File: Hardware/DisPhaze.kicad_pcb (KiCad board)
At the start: 2 copper layers, 60 x 110 mm, 78 parts, among them J1 SWD_Header, J2 PItch_In, J3 PD1_Amt_In, J4 PD2_Amt_In, J5 VCA_In, J6 DAC1_Out, J7 DAC2_Out, J8 Eurorack_16_pin_power, SW1 DAC1_RingMod_Switch, SW2 DAC2_Mix_Switch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

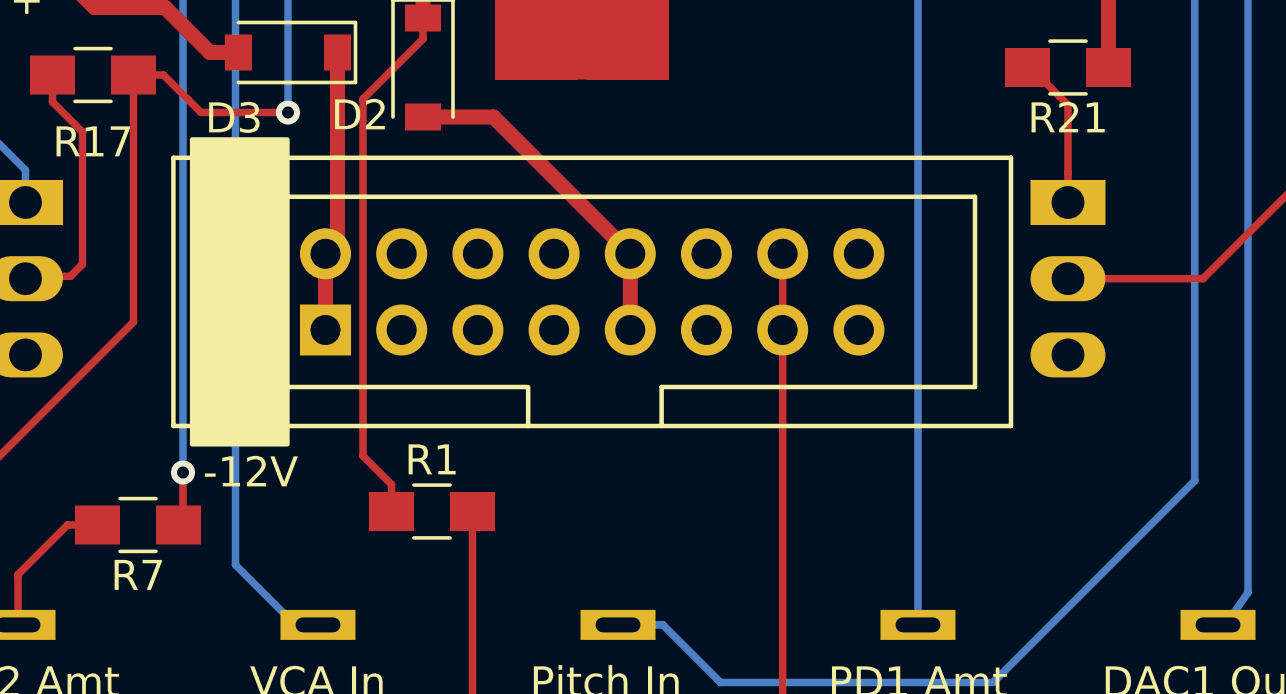
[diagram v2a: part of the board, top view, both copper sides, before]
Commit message: Added 3d models to PCB layout
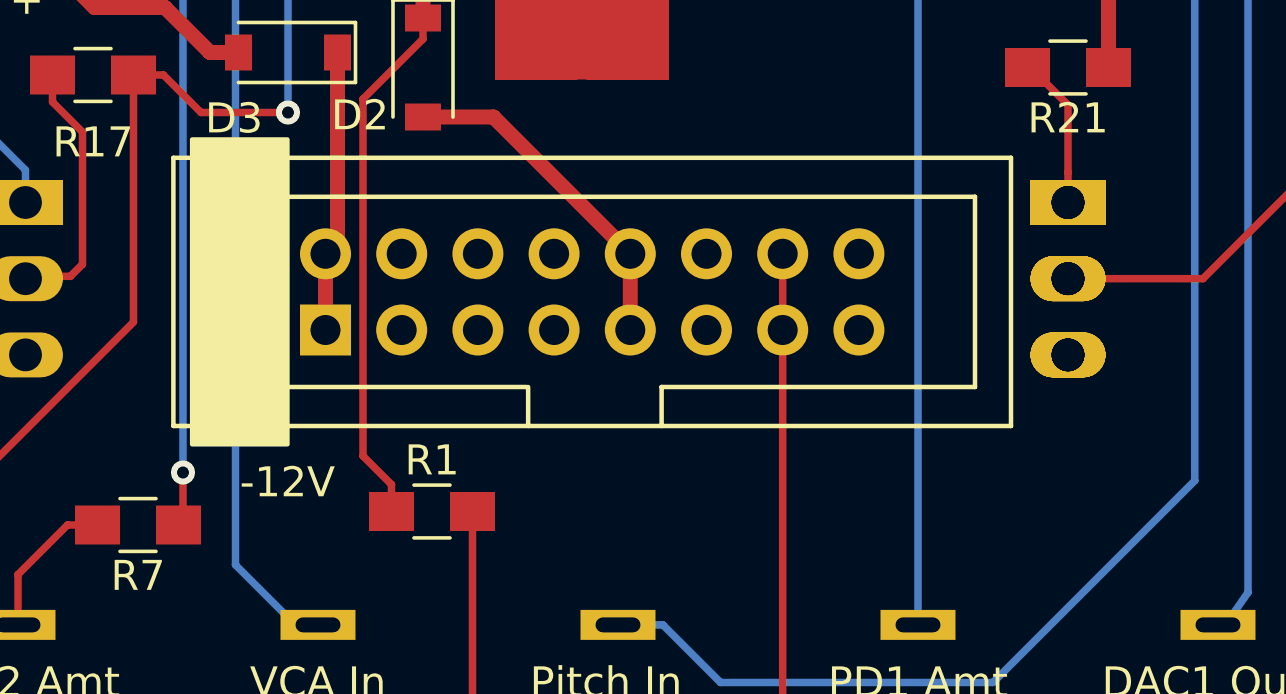
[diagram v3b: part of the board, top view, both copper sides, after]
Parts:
- removed the SW1 at (150.0, 133.0)
- added SW1 (x3): DAC1_RingMod_Switch, Custom_Footprints:SPDTSubMiniature, B.Cu at (150.0, 133.0)
- CTune1, FTune1, PD1Amt1, PD1Type1, PD2Amt1, PD2Type1: footprint Potentiometers:Potentiometer_Alps_RK09K_Horizontal -> Custom_Footprints:Alpha_9mm_Potentiometer
- SW4: footprint Buttons_Switches_SMD:SW_SPST_EVQQ2 -> Custom_Footprints:SW_SPST_EVQQ2
- Y1: footprint Crystals:Crystal_SMD_HC49-SD -> Custom_Footprints:Crystal_SMD

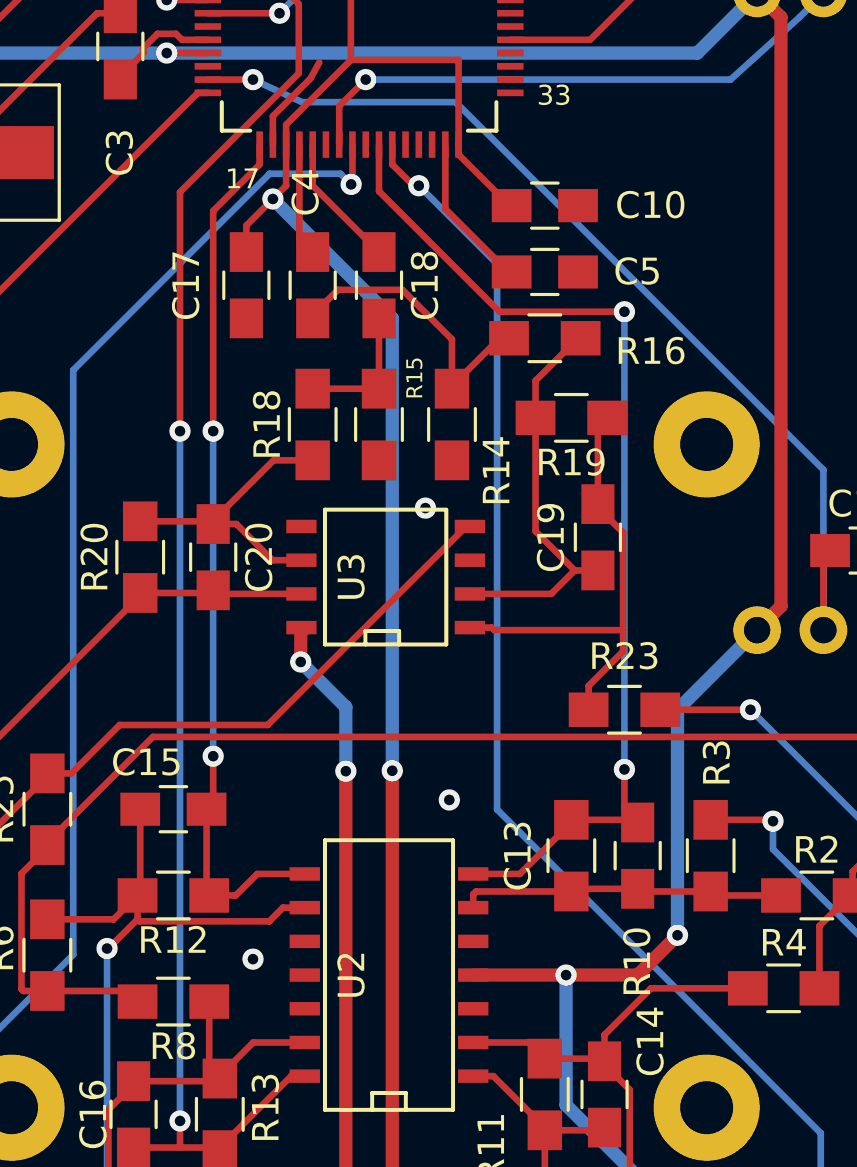
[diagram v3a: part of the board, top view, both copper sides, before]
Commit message: Fixes to PCB silkscreen; Fixes to ADC function
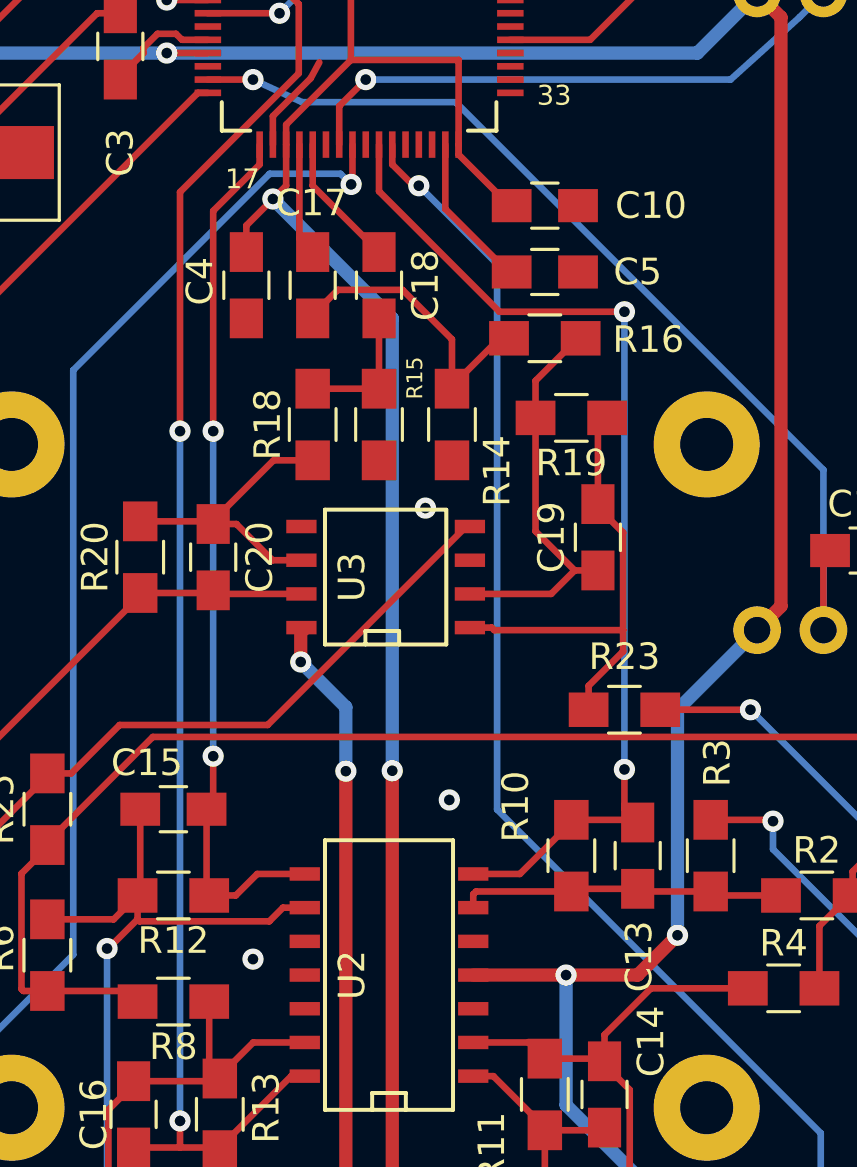
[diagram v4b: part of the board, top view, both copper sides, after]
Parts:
- removed the SW1 at (150.0, 133.0) (x3)
- added SW1 (x3): DAC1_RingMod_Switch, Custom_Footprints:SPDTSubMiniature, B.Cu at (150.0, 133.0)
- C13, C16: value 1nF -> 1.5nF

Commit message: Enabled data and instruction cache; Increased optimizer to O1 for doubling of performance
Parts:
- removed the SW1 at (150.0, 133.0) (x3)
- added SW1 (x3): DAC1_RingMod_Switch, Custom_Footprints:SPDTSubMiniature, B.Cu at (150.0, 133.0)

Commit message: Calibration changes applied immediately; extended readme. Kicad files updated to v6.0
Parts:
- removed the SW1 at (150.0, 133.0) (x3)
- added SW1 (x3): DAC1_RingMod_Switch, Custom_Footprints:SPDTSubMiniature, B.Cu at (150.0, 133.0)
- R16, R18: value 6.3k -> 6.8k
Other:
- net class Default removed
- net class Wide_Power removed
